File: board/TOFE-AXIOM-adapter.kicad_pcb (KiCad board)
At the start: 2 copper layers, 68.9 x 28.3 mm, 4 parts, among them U1 TOFE-8X

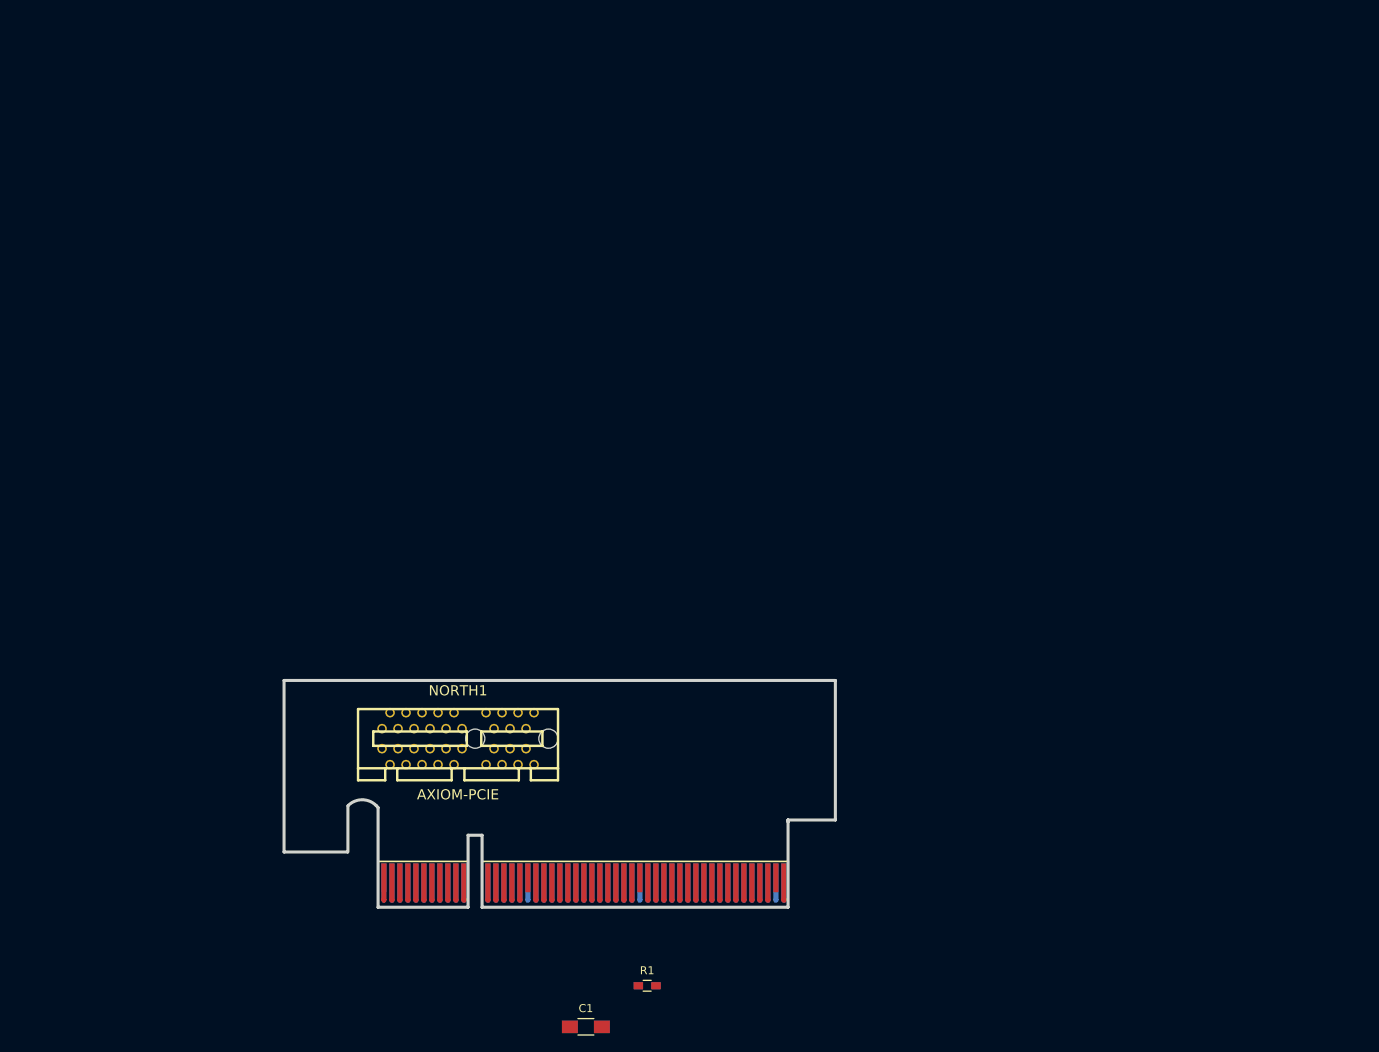
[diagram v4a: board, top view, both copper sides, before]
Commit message: Slowly laying out the PCB.
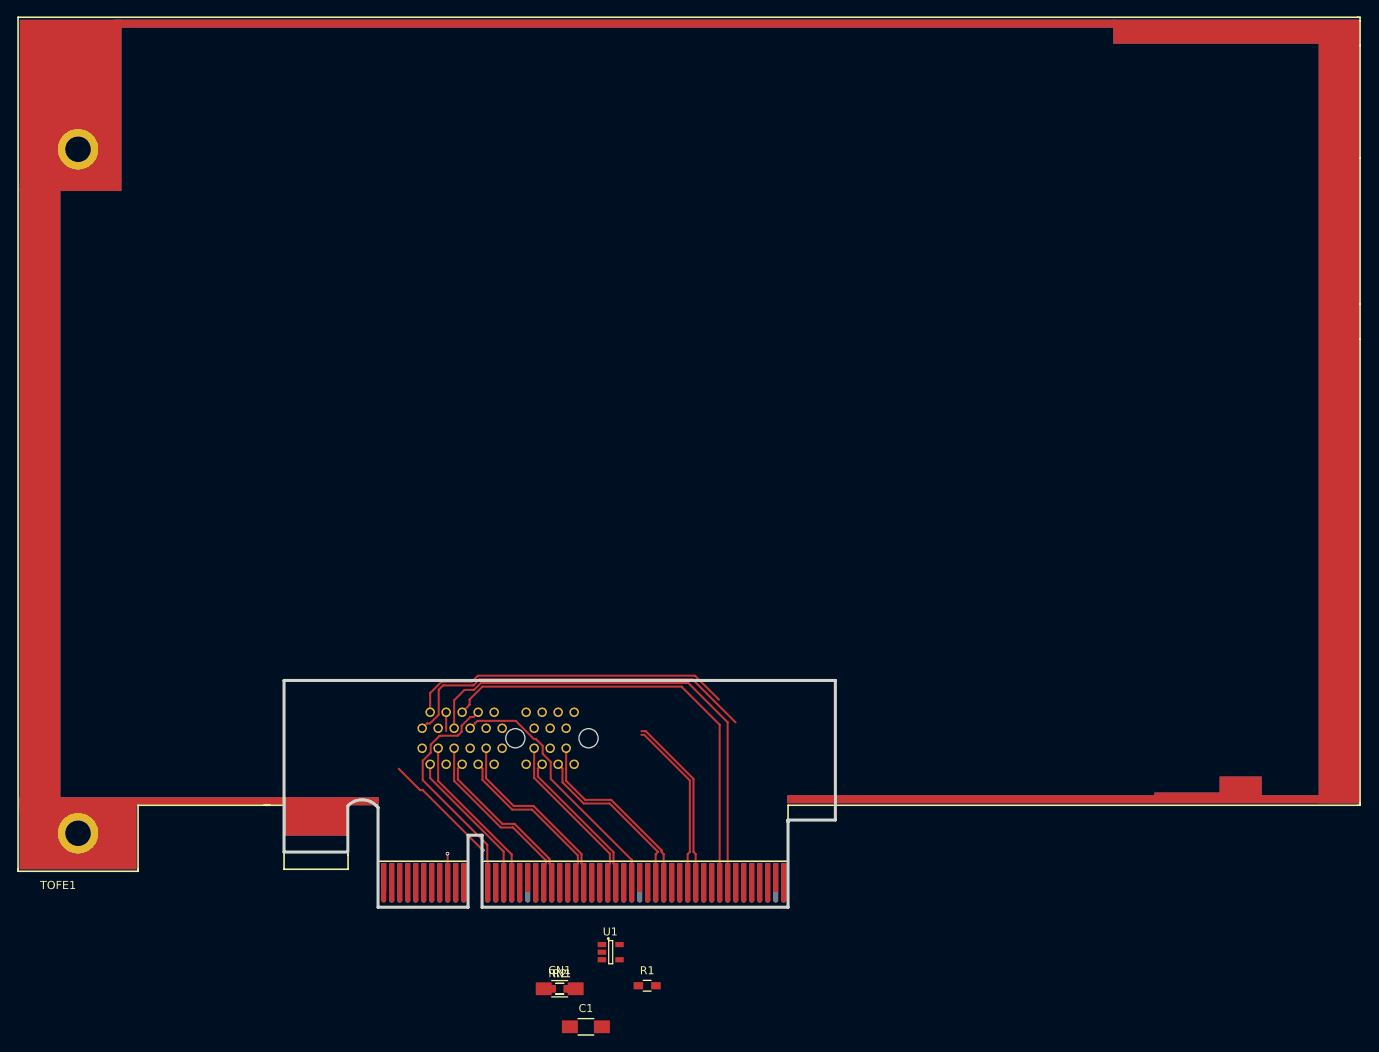
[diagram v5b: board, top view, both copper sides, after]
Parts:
- added CN1: C, Capacitors_SMD:C_1206_HandSoldering, F.Cu at (196.7, 198.3)
- added R2: 10K, Resistors_SMD:R_0603_HandSoldering, F.Cu at (196.7, 198.3)
- added RN1: R, Resistors_SMD:R_0603_HandSoldering, F.Cu at (196.7, 198.3)
- added TOFE1: TOFE-8X, TOFE_8X_HalfHeight:TOFE_8X_HalfHeight, F.Cu at (129.0, 183.7)
- C1: value C -> 0.1uF
- NORTH1: moved to B.Cu
- R1: value R -> 10K
- U1: value TOFE-8X -> 24AA01/24LC01B; footprint TOFE_8X_HL_NW -> TO_SOT_Packages_SMD:SOT-23-5
- moved U1 74.7 mm to (203.1, 193.8)
- moved NORTH1 5.01 mm to (189.0, 167.0)
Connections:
- C1 pad 1: GND -> /VCC3V3
- C1 pad 2: Net-(C1-Pad2) -> GND
- NORTH1 pad A11: Net-(C1-Pad2) -> Net-(CN1-Pad2)
- NORTH1 pad A13: /N_LVDS_A3 -> /N_LVDS_3_P
- NORTH1 pad A14: /N_LVDS_B3 -> /N_LVDS_3_N
- NORTH1 pad A16: /N_LVDS_A4 -> /N_LVDS_4_P
- NORTH1 pad A17: /N_LVDS_B4 -> /N_LVDS_4_N
- NORTH1 pad A2: /N_LVDS_A0 -> /N_LVDS_0_P
- NORTH1 pad A3: /N_LVDS_B0 -> /N_LVDS_0_N
- NORTH1 pad A5: /N_LVDS_A1 -> /N_LVDS_1_P
- NORTH1 pad A6: /N_LVDS_B1 -> /N_LVDS_1_N
- NORTH1 pad A8: /N_LVDS_A2 -> /N_LVDS_2_P
- NORTH1 pad A9: /N_LVDS_B2 -> /N_LVDS_2_N
- NORTH1 pad B16: /N_LVDS_A5 -> /N_LVDS_5_P
- NORTH1 pad B17: /N_LVDS_B5 -> /N_LVDS_5_N
- R1 pad 1: Net-(R1-Pad1) -> /SDA
- R1 pad 2: Net-(C1-Pad2) -> /VCC3V3
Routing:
- net /N_IO1: track 2.30 -> 62.8 mm
- net /N_IO2: track 2.30 -> 57.8 mm
- net /N_SDA: track 2.30 -> 48.4 mm
- net /N_SCL: track 2.30 -> 42.9 mm
- net /N_IO3: track 2.30 -> 34.6 mm
- net /N_IO4: track 2.30 -> 28.9 mm
- net /N_LVDS_4_N: track 0.00 -> 25.9 mm
- net /N_LVDS_2_N: track 0.00 -> 25.5 mm
- net /N_LVDS_5_N: track 0.00 -> 24.3 mm
- net /N_LVDS_4_P: track 0.00 -> 24.2 mm
- net /N_LVDS_2_P: track 0.00 -> 23.7 mm
- net /N_LVDS_5_P: track 0.00 -> 23.5 mm
- net /N_LVDS_3_P: track 0.00 -> 23.0 mm
- net /N_LVDS_1_P: track 0.00 -> 22.4 mm
- net /N_LVDS_3_N: track 0.00 -> 21.2 mm
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
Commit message: Routing.
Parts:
- added CS1: C, Capacitors_SMD:C_1206_HandSoldering, F.Cu at (196.7, 198.3)
- added RS1: R, Resistors_SMD:R_0603_HandSoldering, F.Cu at (196.7, 198.3)
- added SOUTH1: AXIOM-PCIE, w_conn_pc:pci-x_conn-x1, B.Cu at (217.0, 167.1)
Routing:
- net /S_IO5: track 3.51 -> 78.9 mm, vias 1 -> 0
- net /S_IO7: track 0.00 -> 72.1 mm, vias 0 -> 1
- net /S_IO6: track 0.00 -> 66.6 mm, vias 0 -> 1
- net /S_SDA: track 0.00 -> 64.8 mm
- net /S_SCL: track 0.00 -> 63.8 mm
- net /S_IO1: track 0.00 -> 58.4 mm
- net /S_IO2: track 0.00 -> 43.0 mm
- net /N_IO7: track 0.00 -> 41.1 mm
- net /S_IO3: track 0.00 -> 38.3 mm
- net /N_IO6: track 0.00 -> 37.6 mm
- net /S_IO4: track 0.00 -> 36.5 mm, vias 0 -> 1
- net /S_IO0: track 0.00 -> 32.7 mm
- net /S_LVDS_5_P: track 0.00 -> 29.6 mm
- net /S_LVDS_3_P: track 0.00 -> 27.1 mm
- net /S_LVDS_5_N: track 0.00 -> 27.1 mm
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
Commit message: Working on routing.
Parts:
- moved SOUTH1 0.47 mm to (217.4, 166.9)
- moved NORTH1 0.10 mm to (188.9, 166.9)
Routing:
- net /S_SCL: track 63.8 -> 580.1 mm
- net (no net): track 15.2 -> 0.00 mm, vias 1 -> 0
- net GND: track 13.8 -> 0.00 mm
- net /S_IO2: track 43.0 -> 39.3 mm
- net /S_SDA: track 64.8 -> 67.9 mm
- net /N_SCL: track 62.5 -> 60.2 mm
- net /N_LVDS_5_P: track 30.3 -> 28.0 mm
- net /N_LVDS_5_N: track 28.3 -> 26.0 mm
- net /N_LVDS_3_P: track 23.0 -> 20.7 mm
- net /N_LVDS_3_N: track 21.2 -> 18.9 mm
- net /N_LVDS_2_P: track 23.7 -> 21.4 mm
- net /N_LVDS_2_N: track 25.5 -> 23.2 mm
- net /N_IO3: track 34.6 -> 32.3 mm
- net /N_IO2: track 49.7 -> 47.4 mm
- net /N_IO1: track 54.4 -> 52.1 mm
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
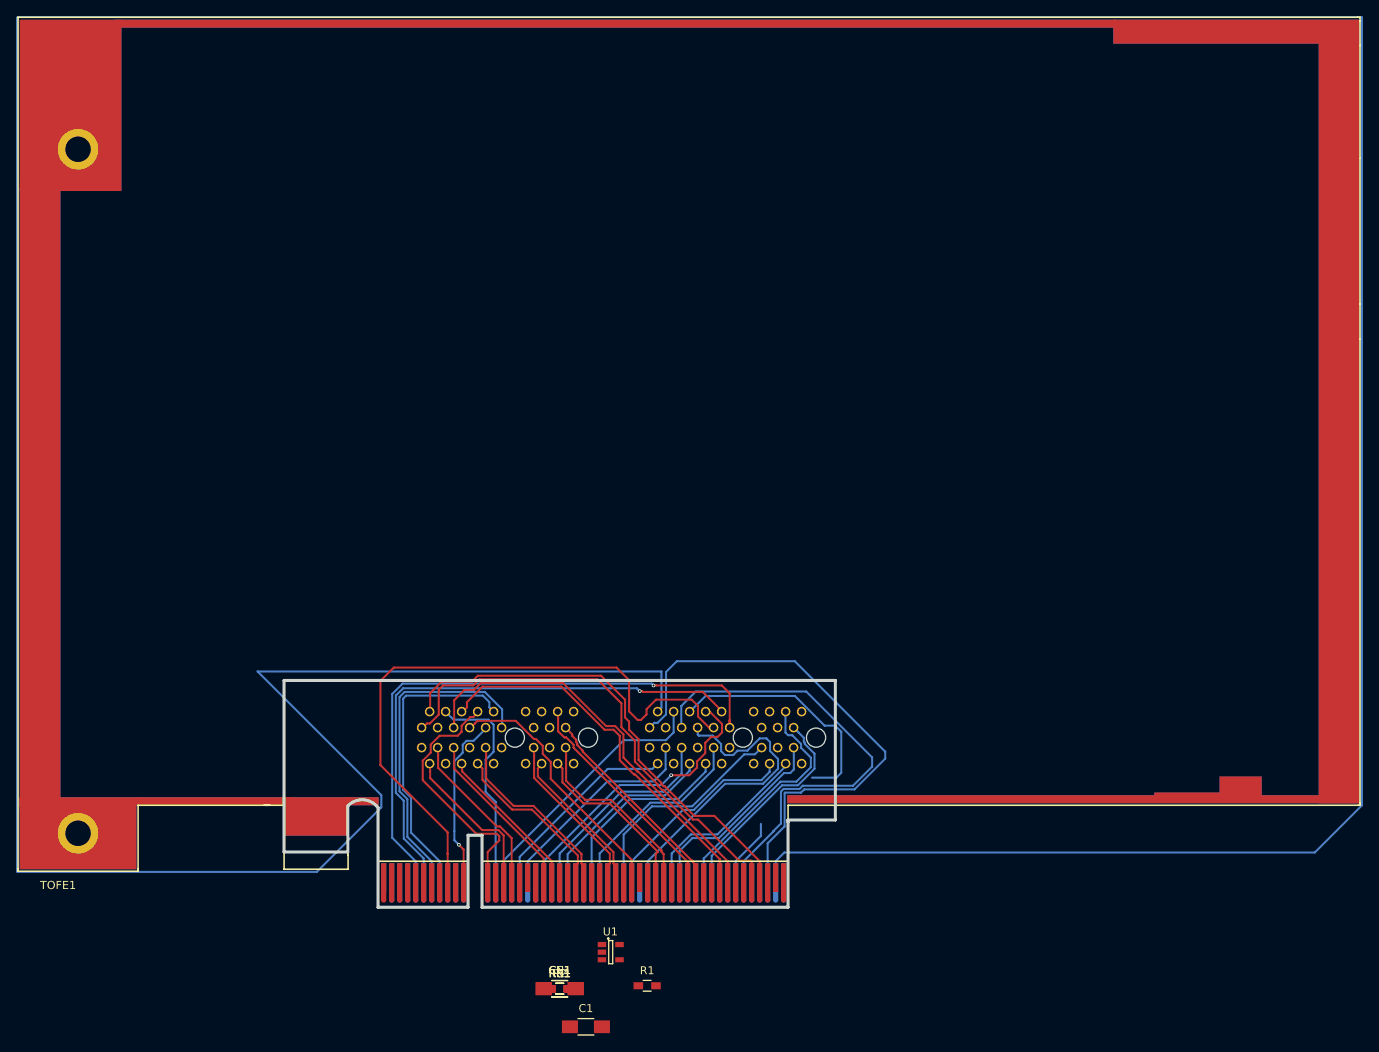
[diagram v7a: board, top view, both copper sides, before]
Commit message: Changing wires to match DRC.
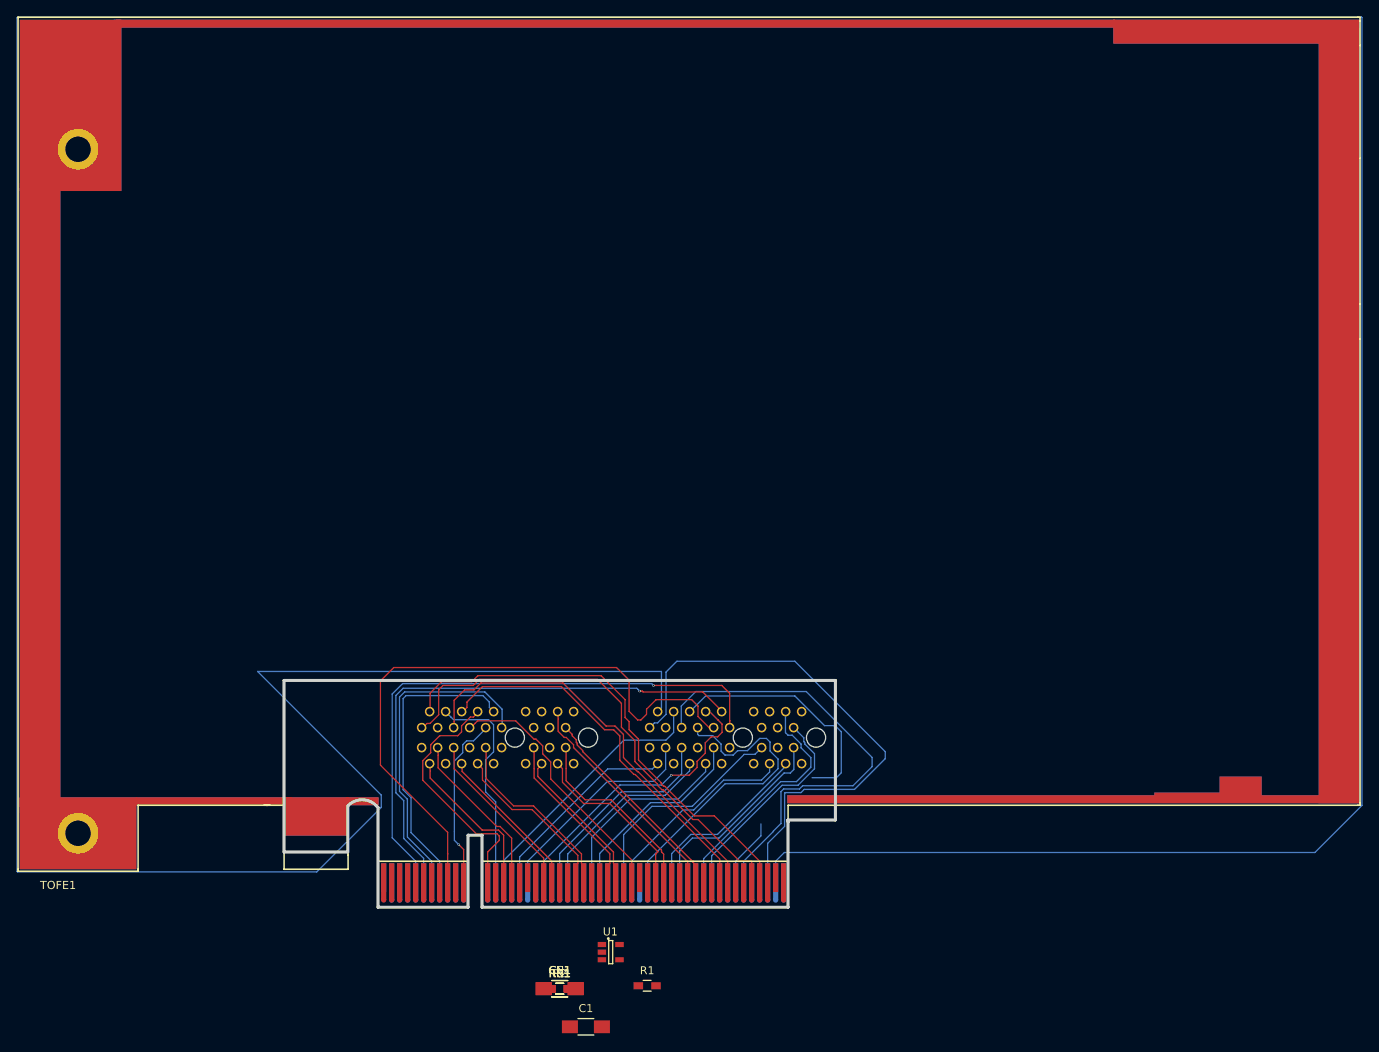
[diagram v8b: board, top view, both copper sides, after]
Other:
- net class Default: trace_width 0.254 -> 0.1524; via_dia 0.4572 -> 0.3048; via_drill 0.254 -> 0.2032
- rule trace_min: 0.005 -> 0.0254
- rule via_min_drill: 0.254 -> 0.1524
- rule via_min_size: 0.018 -> 0.2032
